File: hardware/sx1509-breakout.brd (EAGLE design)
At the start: 25.4 x 35.6 mm, 31 parts, among them U1 SX1509

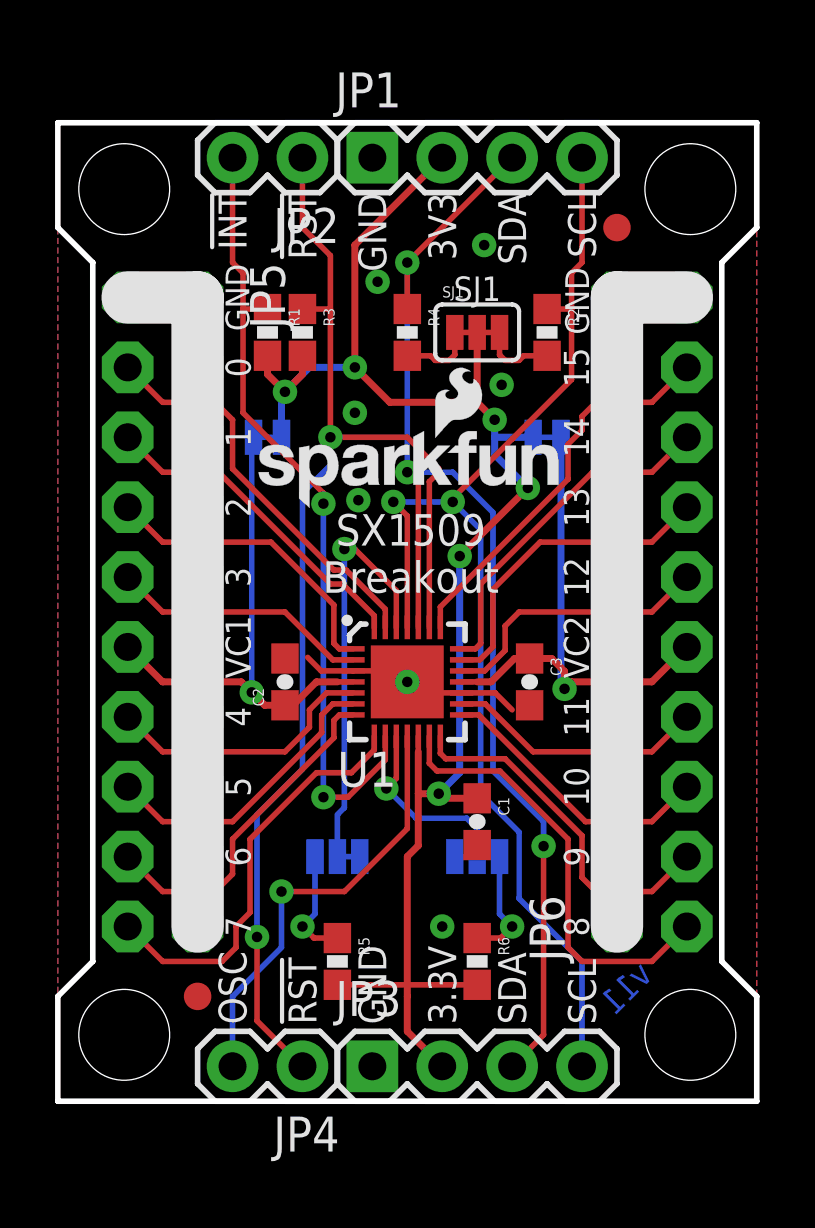
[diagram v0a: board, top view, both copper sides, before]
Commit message: Making power busses selectable. Moving silk.
- Not defaulting the two power bus headers to either GND or VCC.
- Adding two jumpers on each header to allow connecting them high or low.
- This will make it easier to set up LEDs as either source or sink.
- It'll also make it easier to short VCC to GND - will require extra
  caution using the jumpers.
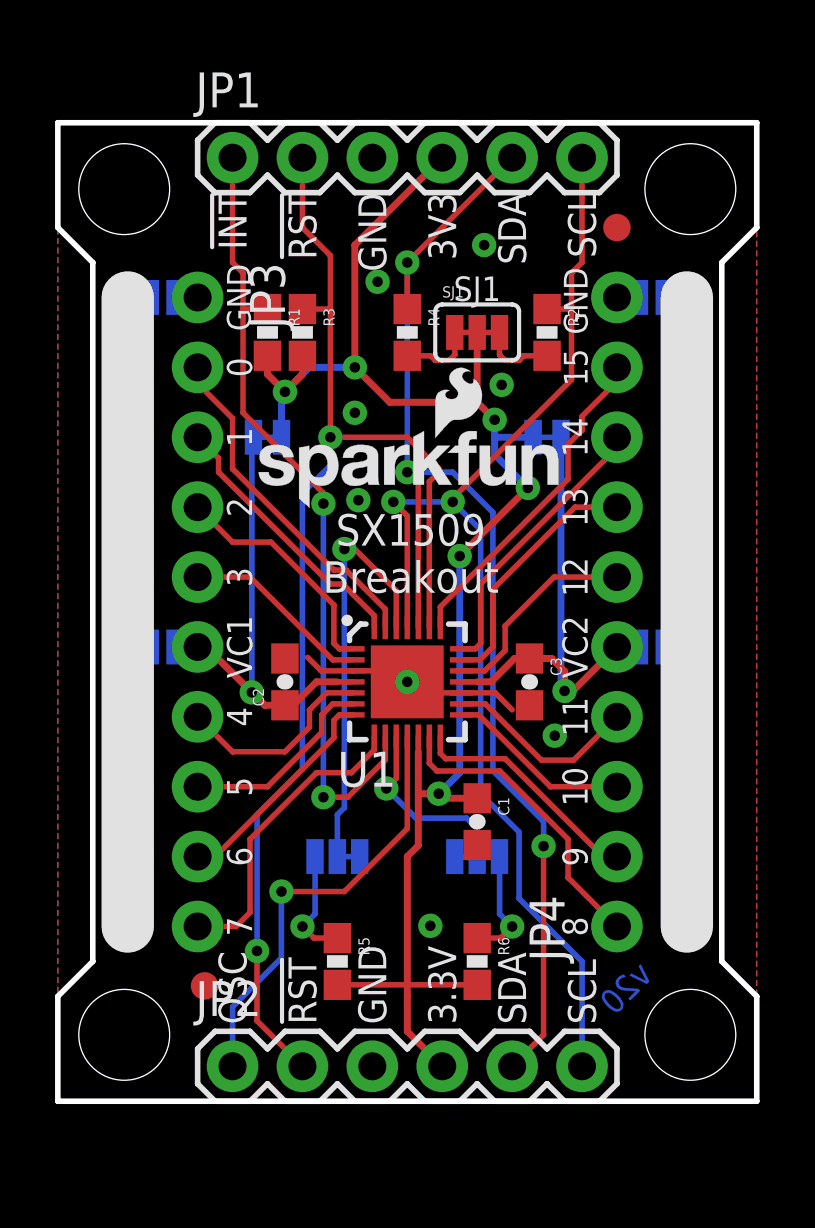
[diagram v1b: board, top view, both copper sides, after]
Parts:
- removed JP5, JP6: (no value), SparkFun-Connectors:2X10_NOSILK
- added SJ6: A-VCC1, SparkFun-Passives:PAD-JUMPER-2-NO_NO_SILK
- added SJ7: A-GND, SparkFun-Passives:PAD-JUMPER-2-NO_NO_SILK
- added SJ8: B-VCC2, SparkFun-Passives:PAD-JUMPER-2-NO_NO_SILK
- added SJ9: B-GND, SparkFun-Passives:PAD-JUMPER-2-NO_NO_SILK
- JP1: device SparkFun-Connectors:1X04 -> SparkFun-Connectors:1X06
- JP2: device SparkFun-Connectors:1X02 -> SparkFun-Connectors:1X06
- JP3: device SparkFun-Connectors:1X04 -> SparkFun-Connectors:2X10_ROUND_NOSILK
- JP4: device SparkFun-Connectors:1X02 -> SparkFun-Connectors:2X10_ROUND_NOSILK
- moved JP2 33.1 mm to (6.35, 1.27), turned to 0 degrees
- moved JP4 20.8 mm to (21.6, 17.8), turned to 90 degrees
- moved JP3 18.2 mm to (3.81, 17.8), turned to 270 degrees
- moved JP1 5.08 mm to (6.35, 34.3)
- moved JP10 0.46 mm to (5.33, 4.19)
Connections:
- new net N$3: JP4.1, JP4.11, JP4.13, JP4.15, JP4.17, JP4.19, JP4.3, JP4.5, JP4.7, JP4.9, SJ8.1, SJ9.1
- new net PWRBUSA: JP3.1, JP3.11, JP3.13, JP3.15, JP3.17, JP3.19, JP3.3, JP3.5, JP3.7, JP3.9, SJ6.1, SJ7.1
- net !INT: now also JP1.1; no longer JP2.2
- net !RESET: now also JP1.2, JP2.2; no longer JP2.1, JP4.1
- net 0: now also JP3.4; no longer JP5.3
- net 1: now also JP3.6; no longer JP5.5
- net 10: now also JP4.6; no longer JP6.5
- net 11: now also JP4.8; no longer JP6.7
- net 12: now also JP4.12; no longer JP6.11
- net 13: now also JP4.14; no longer JP6.13
- net 14: now also JP4.16; no longer JP6.15
- net 15: now also JP4.18; no longer JP6.17
- net 2: now also JP3.8; no longer JP5.7
- net 3: now also JP3.10; no longer JP5.9
- net 3.3V: now also JP1.4, JP2.4; no longer JP1.2, JP3.2
- net 4: now also JP3.14; no longer JP5.13
- net 5: now also JP3.16; no longer JP5.15
- net 6: now also JP3.18; no longer JP5.17
- net 7: now also JP3.20; no longer JP5.19
- net 8: now also JP4.2; no longer JP6.1
- net 9: now also JP4.4; no longer JP6.3
- net GND: now also JP1.3, JP2.3, JP3.2, JP4.20, SJ7.2, SJ9.2; no longer JP1.1, JP3.1, JP5.1, JP5.10, JP5.12, JP5.14, JP5.16, JP5.18, JP5.2, JP5.20, JP5.4, JP5.6, JP5.8, JP6.10, JP6.12, JP6.14, JP6.16, JP6.18, JP6.19, JP6.2, JP6.20, JP6.4, JP6.6, JP6.8
- net OSCIO: now also JP2.1; no longer JP4.2
- net SCL: now also JP1.6, JP2.6; no longer JP1.4, JP3.4
- net SDA: now also JP1.5, JP2.5; no longer JP1.3, JP3.3
- net VCC1: now also JP3.12, SJ6.2; no longer JP5.11
- net VCC2: now also JP4.10, SJ8.2; no longer JP6.9
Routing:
- net PWRBUSA: track 0.00 -> 24.5 mm
- net N$3: track 0.00 -> 24.5 mm
- net 8: track 16.2 -> 11.1 mm
- net 9: track 13.1 -> 8.60 mm
- net 6: track 12.5 -> 8.15 mm
- net 7: track 15.2 -> 11.1 mm
- net 5: track 10.9 -> 7.26 mm
- net 10: track 10.3 -> 6.73 mm
- net 2: track 11.1 -> 8.60 mm
- net 4: track 9.97 -> 7.43 mm
- net 3: track 9.43 -> 6.89 mm
- net 13: track 11.7 -> 9.17 mm
- net 12: track 10.1 -> 7.58 mm
- net 14: track 12.6 -> 10.3 mm
- net 11: track 9.43 -> 7.14 mm
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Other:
- board text added: "v20"
- board text removed: "v11"

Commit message: Defaulting power busses to GND. Moving SJ2&3.
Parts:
- SJ2: value (none) -> VCC1-3.3V
- SJ3: value (none) -> VCC2-3.3V
- SJ7: value A-GND -> GND; device SparkFun-Passives:PAD-JUMPER-2-NO_NO_SILK -> SparkFun-Passives:PAD-JUMPER-2-NC_BY_TRACE_NO_SILK
- SJ9: value B-GND -> GND; device SparkFun-Passives:PAD-JUMPER-2-NO_NO_SILK -> SparkFun-Passives:PAD-JUMPER-2-NC_BY_TRACE_NO_SILK
- moved SJ2 1.80 mm to (8.89, 25.4)
- moved SJ3 1.80 mm to (16.5, 25.4)
- moved LOGO3 0.36 mm to (15.9, 27.9)
- moved LOGO2 0.28 mm to (10.3, 26.4)
- turned SJ7 to 0 degrees
- turned SJ9 to 180 degrees
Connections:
- net GND: now also SJ7.1, SJ9.1; no longer SJ7.2, SJ9.2
- net N$3: now also SJ9.2; no longer SJ9.1
- net PWRBUSA: now also SJ7.2; no longer SJ7.1
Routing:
- net VCC2: track 17.7 -> 19.9 mm
- net GND: track 9.02 -> 10.5 mm, vias 8 -> 9
- net 3.3V: track 62.3 -> 63.7 mm
- net VCC1: track 17.0 -> 18.4 mm
- net 0: track 12.5 -> 13.4 mm
- net 2: track 8.60 -> 7.78 mm
- net 1: track 9.83 -> 10.7 mm
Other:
- board text added: "V"
